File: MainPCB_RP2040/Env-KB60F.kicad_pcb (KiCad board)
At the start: 2 copper layers, 283 x 126.5 mm, 177 parts, among them J1 SKRKAEE020, J2 SKRKAEE020, J5 Conn_01x03_Male, U1 TLV75533PDBVR, U3 RP2040, Y1 3225_4P

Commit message: finished up RP2040 version, need to fill the blank space.
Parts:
- removed J5: Conn_01x03_Male, Connector_PinHeader_2.54mm:PinHeader_1x03_P2.54mm_Horizontal
- added REF**: KiCad-Logo_6mm_Copper, Symbol:KiCad-Logo_6mm_Copper, B.Cu at (303.5, 38.4)
- moved J1 17.6 mm to (357.7, 50.4), turned to 90 degrees
- moved C13 0.42 mm to (331.4, 49.5)
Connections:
- U3 pad 11: (no net) -> col3
- U3 pad 12: (no net) -> col4
- U3 pad 13: (no net) -> col5
- U3 pad 14: (no net) -> col6
- U3 pad 15: (no net) -> col7
- U3 pad 16: (no net) -> col8
- U3 pad 17: (no net) -> col9
- U3 pad 18: (no net) -> col10
- U3 pad 2: (no net) -> row4
- U3 pad 27: (no net) -> col11
- U3 pad 28: (no net) -> col12
- U3 pad 29: (no net) -> col13
- U3 pad 3: (no net) -> row3
- U3 pad 30: (no net) -> col14
- U3 pad 4: (no net) -> row2
- U3 pad 5: (no net) -> row1
- U3 pad 6: (no net) -> row0
- U3 pad 7: (no net) -> col0
- U3 pad 8: (no net) -> col1
- U3 pad 9: (no net) -> col2
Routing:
- net row4: track 215.7 -> 248.6 mm, vias 0 -> 1
- net col6: track 205.0 -> 234.5 mm, vias 0 -> 1
- net col7: track 204.9 -> 232.4 mm, vias 0 -> 1
- net row0: track 223.8 -> 250.3 mm, vias 0 -> 1
- net row3: track 221.6 -> 247.0 mm, vias 0 -> 1
- net col0: track 332.1 -> 357.2 mm, vias 0 -> 1
- net col1: track 297.3 -> 322.2 mm, vias 0 -> 1
- net col2: track 268.0 -> 292.8 mm, vias 0 -> 1
- net col3: track 273.4 -> 298.2 mm, vias 0 -> 1
- net col4: track 229.6 -> 253.9 mm, vias 0 -> 1
- net col5: track 243.5 -> 267.8 mm, vias 0 -> 1
- net col8: track 156.8 -> 177.8 mm, vias 0 -> 1
- net row2: track 225.1 -> 246.0 mm, vias 0 -> 2
- net row1: track 227.4 -> 248.0 mm, vias 0 -> 1
- net col11: track 126.2 -> 146.1 mm, vias 0 -> 1
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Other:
- board text added: "BOOTSEL"
- board text added: "RESET"
- board text removed: ">"

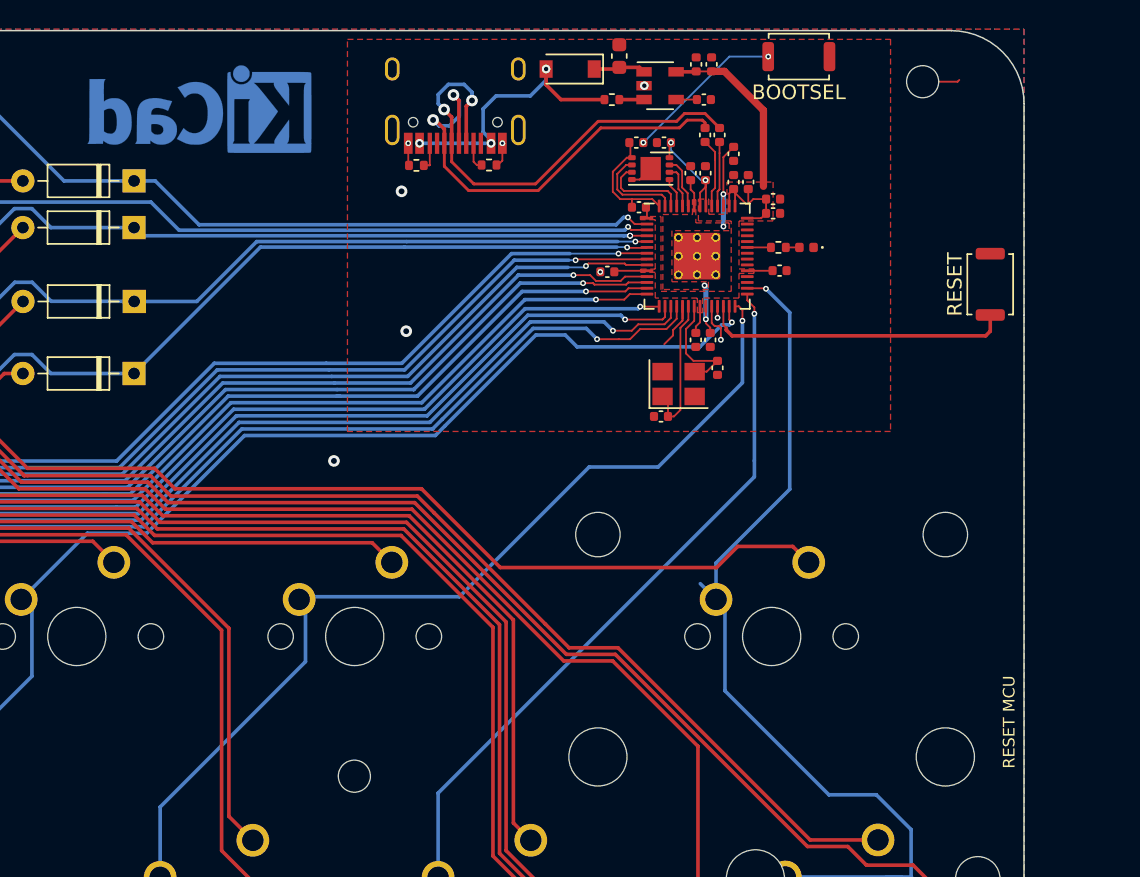
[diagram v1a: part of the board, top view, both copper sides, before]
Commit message: finished up RP2040 version some more, added debug header and spare GPIO header.
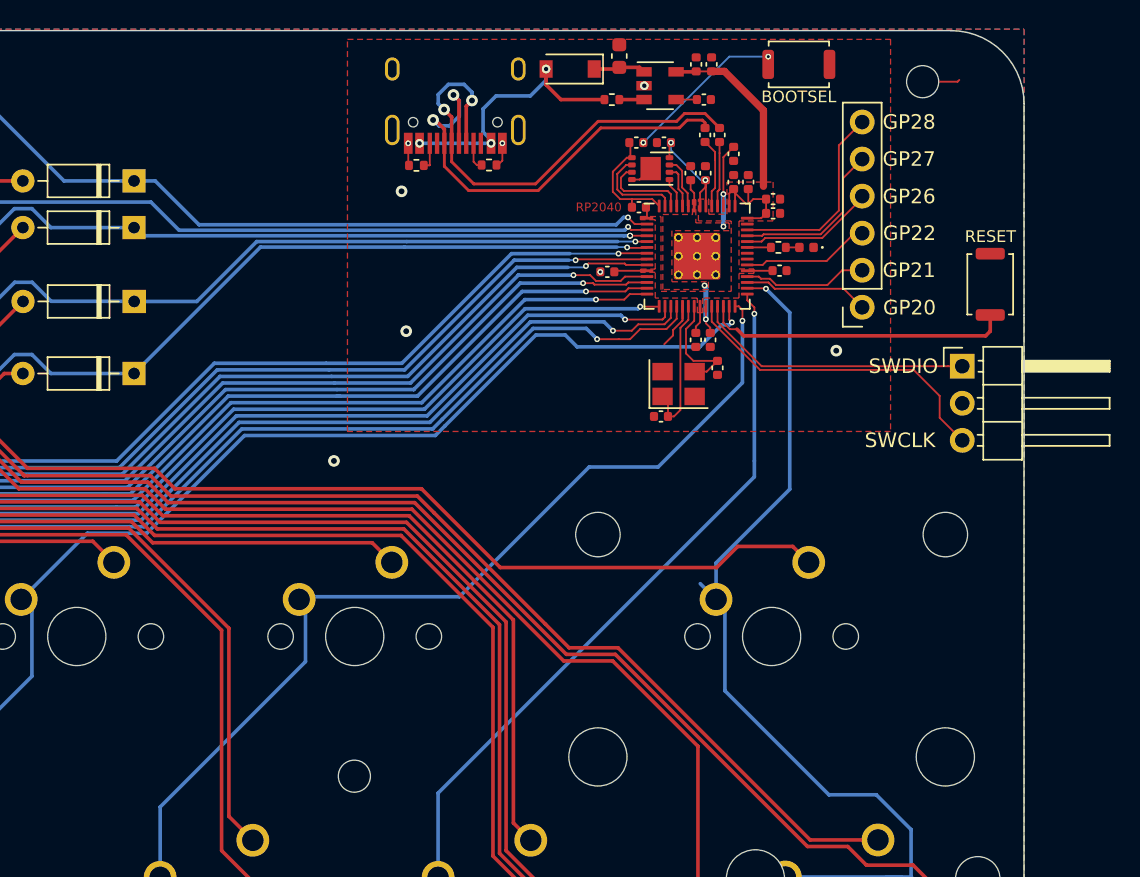
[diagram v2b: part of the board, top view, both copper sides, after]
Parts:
- removed REF**: KiCad-Logo_6mm_Copper, Symbol:KiCad-Logo_6mm_Copper
- added J3: Conn_01x06, Connector_PinSocket_2.54mm:PinSocket_1x06_P2.54mm_Vertical, F.Cu at (348.9, 52.0)
- added J5: Conn_01x03_Male, Connector_PinHeader_2.54mm:PinHeader_1x03_P2.54mm_Horizontal, F.Cu at (355.8, 56.0)
- moved J2 0.53 mm to (344.6, 35.3)
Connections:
- U3 pad 31: (no net) -> GP20
- U3 pad 32: (no net) -> GP21
- U3 pad 34: (no net) -> GP22
- U3 pad 38: (no net) -> GP26
- U3 pad 39: (no net) -> GP27
- U3 pad 40: (no net) -> GP28
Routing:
- net /SWCLK: track 2.73 -> 22.5 mm, vias 1 -> 0
- net /SWD: track 0.78 -> 19.1 mm, vias 1 -> 0
- net GP28: track 0.00 -> 13.6 mm
- net GP27: track 0.00 -> 11.4 mm
- net GP26: track 0.00 -> 9.24 mm
- net GP22: track 0.00 -> 8.78 mm
- net GP20: track 0.00 -> 8.58 mm
- net GP21: track 0.00 -> 8.54 mm
- net GND: vias 7 -> 8
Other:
- board text added: "GP20"
- board text added: "GP21"
- board text added: "GP22"
- board text added: "GP26"
- board text added: "GP27"
- board text added: "GP28"
- board text added: "RP2040"
- board text added: "SWCLK"
- board text added: "SWDIO"
- board text removed: "RESET MCU"

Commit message: Corrected mount hole placement on all PCBs and updated the switch plate to fit triple spacebar split.
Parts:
- moved H1 5.00 mm to (227.5, 155.0)

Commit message: updated git ignore to allow BOM/CPL and updated readme.
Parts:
- added REF**: KiCad-Logo_6mm_Copper, Symbol:KiCad-Logo_6mm_Copper, B.Cu at (304.2, 38.2)
- added REF**: OSHW-Logo_11.4x12mm_Copper, Symbol:OSHW-Logo_11.4x12mm_Copper, B.Cu at (85.8, 49.6)
- moved C1 2.44 mm to (334.6, 34.2), turned to 0 degrees
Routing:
- net VSYS: track 3.58 -> 5.20 mm

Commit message: tested some logos and placements to fill empty space, might relocate the MCU setup a bit.
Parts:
- removed the G*** at (87.2, 47.5)
- removed K_27: KEYSW, MX_Only:MXOnly-1U-NoLED
- added G***: LOGO, Logo:logotest1, F.Cu at (316.9, 52.0)
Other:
- board text added: "Raspberry Pi RP2040"
- board text removed: "RP2040"
